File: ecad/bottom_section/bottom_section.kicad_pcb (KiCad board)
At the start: 2 copper layers, 100 x 57 mm, 50 parts, among them J1 JST PH 3, J3 JST PH 3, J5 Conn_01x08, SW1 SW_Push, SW10 SW_Push, SW2 SW_Push, SW3 SW_Push, SW4 SW_Push, SW5 SW_Push, SW6 SW_Push, SW7 SW_Push, SW8 SW_Push, SW9 SW_Push

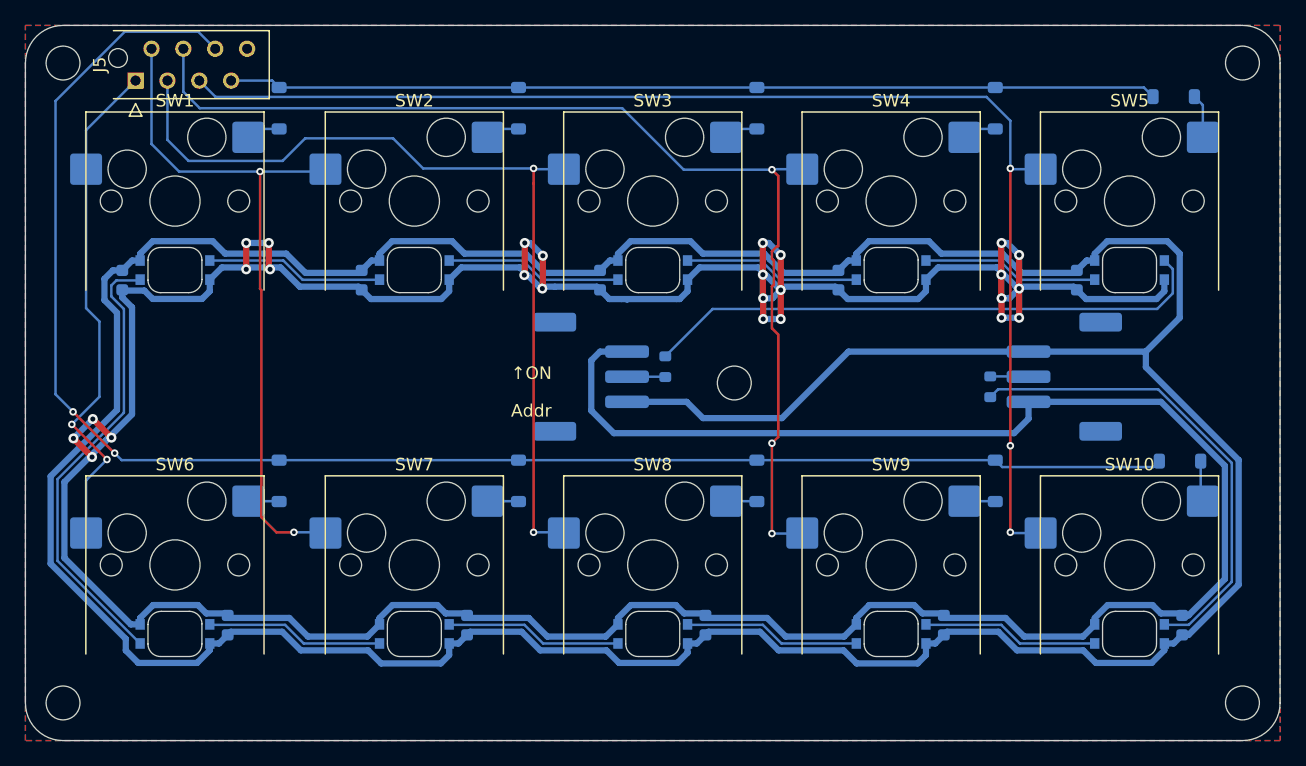
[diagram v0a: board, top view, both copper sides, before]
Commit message: Uses LED Matrix controller on all board.
It simplifies so much the design for a small cost.
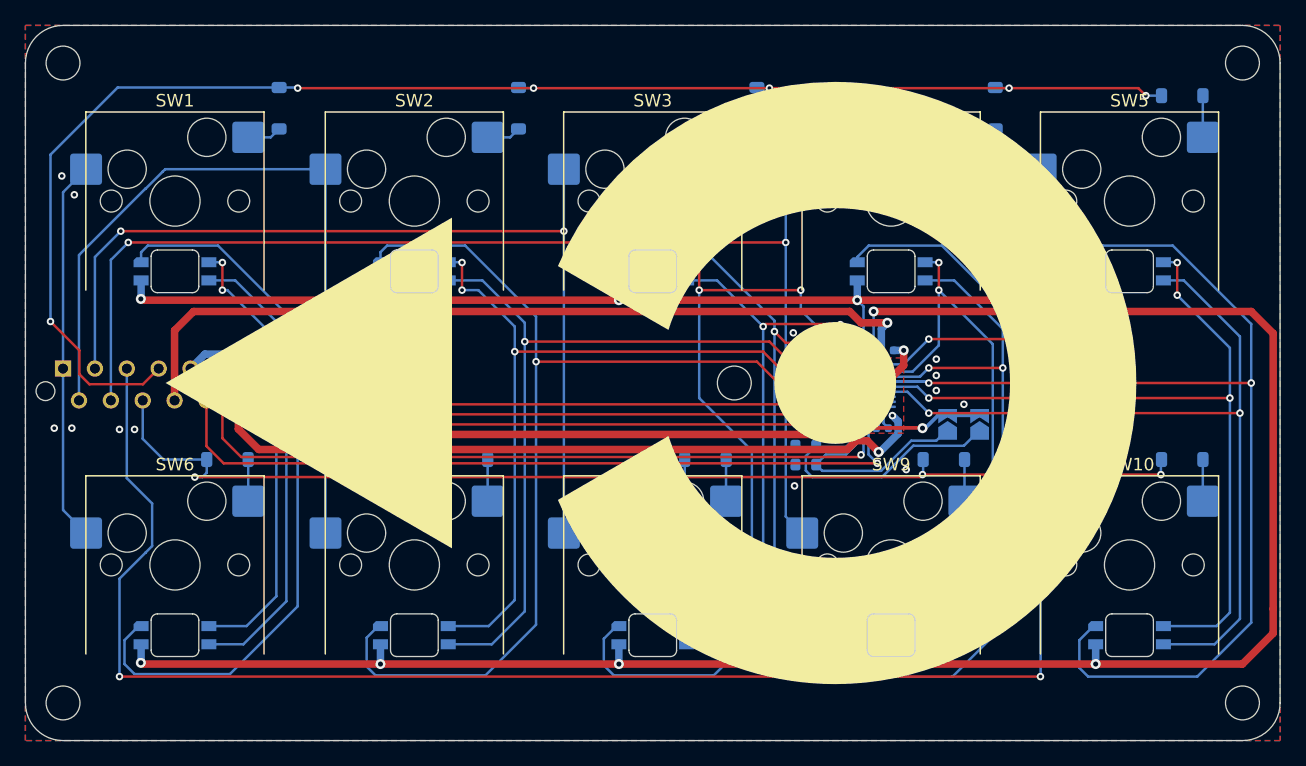
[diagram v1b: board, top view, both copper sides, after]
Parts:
- removed C1, C10, C6, C7, C8, C9: 100n, Capacitor_SMD:C_0603_1608Metric
- removed J3: JST PH 3, woodpecker:JST_PH_S3B-PH-SM4-TB_1x03-1MP_P2.00mm_Horizontal
- removed J5: Conn_01x08, Connector_TE-Connectivity:TE_Micro-MaTch_215079-8_2x04_P1.27mm_Vertical
- removed R7, R8: 33, Resistor_SMD:R_0603_1608Metric
- added JP1: SolderJumper_2_Open, Jumper:SolderJumper-2_P1.3mm_Open_TrianglePad1.0x1.5mm, B.Cu at (123.5, 58.8)
- added JP2: SolderJumper_2_Open, Jumper:SolderJumper-2_P1.3mm_Open_TrianglePad1.0x1.5mm, B.Cu at (126.0, 58.8)
- added R1: 10k, Resistor_SMD:R_0603_1608Metric, B.Cu at (112.2, 62.0)
- added R2: 10k, Resistor_SMD:R_0603_1608Metric, B.Cu at (112.2, 60.5)
- added REF**: OSHW-Logo_11.4x12mm_SilkScreen, Symbol:OSHW-Logo_11.4x12mm_SilkScreen, B.Cu at (90.9, 77.3)
- added U2: LP5864, woodpecker:Texas_LP586X_VQFN-32-1EP_4x4mm_P0.4mm_EP2.8x2.8mm_ThermalVias, B.Cu at (117.0, 56.0)
- added kibuzzard-68CC277E: G***, kibuzzard-68CC277E, B.Cu at (124.8, 56.4)
- added kibuzzard-68CC27A1: G***, kibuzzard-68CC27A1, B.Cu at (127.9, 60.1)
- added kibuzzard-68CC27B2: G***, kibuzzard-68CC27B2, B.Cu at (131.1, 58.8)
- added kibuzzard-68CC27E6: G***, kibuzzard-68CC27E6, B.Cu at (60.0, 51.2)
- added kibuzzard-68CC2926: G***, kibuzzard-68CC2926, B.Cu at (141.1, 53.3)
- C2, C3, C5: value 100n -> 1u; footprint Capacitor_SMD:C_0603_1608Metric -> Capacitor_SMD:C_0402_1005Metric
- C4: value 100n -> 1n; footprint Capacitor_SMD:C_0603_1608Metric -> Capacitor_SMD:C_0402_1005Metric
- D1, D11, D13, D15, D17, D19, D3, D5, D7, D9: value IN-PI32TAR -> LED_BGRA; footprint woodpecker:LED_Inolux_IN-PI32TAR_PLCC4_3.2x2.8mm_P1.5mm -> woodpecker:LED_Inolux_IN-PI32TRRRGB_PLCC4_3.2x2.8mm_P1.5mm
- J1: value JST PH 3 -> Micro-MaTch 2x06; footprint woodpecker:JST_PH_S3B-PH-SM4-TB_1x03-1MP_P2.00mm_Horizontal -> Connector_TE-Connectivity:TE_Micro-MaTch_1-215079-2_2x06_P1.27mm_Vertical
- moved J1 42.1 mm to (53.0, 54.4), turned to -90 degrees
- moved C2 38.4 mm to (113.5, 58.6)
- moved C3 23.6 mm to (118.7, 52.9), turned to 0 degrees
- moved C5 19.5 mm to (118.3, 59.1), turned to 180 degrees
- moved C4 11.8 mm to (114.9, 59.1), turned to 180 degrees
- moved D12 4.46 mm to (66.1, 61.6), turned to 0 degrees
- moved D14 4.44 mm to (85.2, 61.6), turned to 0 degrees
- moved D16 4.44 mm to (104.2, 61.6), turned to 0 degrees
- moved D18 4.44 mm to (123.2, 61.6), turned to 0 degrees
- moved D10 0.68 mm to (142.2, 32.6)
- moved D20 0.22 mm to (142.2, 61.6)
- moved D1 0.10 mm to (61.9, 46.6), turned to 180 degrees
- moved D3 0.10 mm to (81.0, 46.6), turned to 180 degrees
- moved D5 0.10 mm to (100.0, 46.6), turned to 180 degrees
- moved D7 0.10 mm to (119.0, 46.6), turned to 180 degrees
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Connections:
- C2 pad 1: +5V -> +3V3
- C4 pad 1: +5V -> +3V3
- C5 pad 1: +5V -> Net-(U2-VCAP)
- D1 pad 1: +5V -> /C1_LEDB
- D1 pad 2: /KeyboardKey_COL1/DOUT -> /C1_LEDG
- D1 pad 3: GND -> /C1_LEDR
- D1 pad 4: /KeyboardKey_COL1/DIN -> /R5_LEDA
- D11 pad 1: +5V -> /C1_LEDB
- D11 pad 2: /KeyboardKey_COL6/DOUT -> /C1_LEDG
- D11 pad 3: GND -> /C1_LEDR
- D11 pad 4: /KeyboardKey_COL1/DOUT -> /R6_LEDA
- D13 pad 1: +5V -> /C2_LEDB
- D13 pad 2: /KeyboardKey_COL7/DOUT -> /C2_LEDG
- D13 pad 3: GND -> /C2_LEDR
- D13 pad 4: /KeyboardKey_COL6/DOUT -> /R6_LEDA
- D15 pad 1: +5V -> /C3_LEDB
- D15 pad 2: /KeyboardKey_COL8/DOUT -> /C3_LEDG
- D15 pad 3: GND -> /C3_LEDR
- D15 pad 4: /KeyboardKey_COL7/DOUT -> /R6_LEDA
- D17 pad 1: +5V -> /C4_LEDB
- D17 pad 2: /KeyboardKey_COL10/DIN -> /C4_LEDG
- D17 pad 3: GND -> /C4_LEDR
- D17 pad 4: /KeyboardKey_COL8/DOUT -> /R6_LEDA
- D19 pad 1: +5V -> /C5_LEDB
- D19 pad 2: /KeyboardKey_COL10/DOUT -> /C5_LEDG
- D19 pad 3: GND -> /C5_LEDR
- D19 pad 4: /KeyboardKey_COL10/DIN -> /R6_LEDA
- D3 pad 1: +5V -> /C2_LEDB
- D3 pad 2: /KeyboardKey_COL1/DIN -> /C2_LEDG
- D3 pad 3: GND -> /C2_LEDR
- D3 pad 4: /KeyboardKey_COL2/DIN -> /R5_LEDA
- D5 pad 1: +5V -> /C3_LEDB
- D5 pad 2: /KeyboardKey_COL2/DIN -> /C3_LEDG
- D5 pad 3: GND -> /C3_LEDR
- D5 pad 4: /KeyboardKey_COL3/DIN -> /R5_LEDA
- D7 pad 1: +5V -> /C4_LEDB
- D7 pad 2: /KeyboardKey_COL3/DIN -> /C4_LEDG
- D7 pad 3: GND -> /C4_LEDR
- D7 pad 4: /KeyboardKey_COL4/DIN -> /R5_LEDA
- D9 pad 1: +5V -> /C5_LEDB
- D9 pad 2: /KeyboardKey_COL4/DIN -> /C5_LEDG
- D9 pad 3: GND -> /C5_LEDR
- D9 pad 4: /KeyboardKey_COL5/DIN -> /R5_LEDA
- J1 pad 1: +5V -> /COL1
- J1 pad 2: /DIN -> /COL2
- J1 pad 3: GND -> /COL3
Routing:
- net GND: track 350.3 -> 74.9 mm, vias 26 -> 19
- net +5V: track 308.8 -> 67.0 mm, vias 0 -> 1
- net /R6_LEDA: track 0.00 -> 159.8 mm, vias 0 -> 6
- net /C1_LEDB: track 0.00 -> 102.7 mm, vias 0 -> 2
- net /C5_LEDB: track 0.00 -> 91.3 mm, vias 0 -> 2
- net /R5_LEDA: track 0.00 -> 89.2 mm, vias 0 -> 5
- net /C2_LEDB: track 0.00 -> 84.7 mm, vias 0 -> 2
- net /C1_LEDG: track 0.00 -> 81.7 mm, vias 0 -> 4
- net /C1_LEDR: track 0.00 -> 81.6 mm, vias 0 -> 2
- net +3V3: track 0.00 -> 73.5 mm, vias 0 -> 3
- net /C4_LEDB: track 0.00 -> 70.5 mm, vias 0 -> 2
- net /C5_LEDR: track 0.00 -> 65.9 mm, vias 0 -> 2
- net /C3_LEDB: track 0.00 -> 65.8 mm, vias 0 -> 2
- net /C2_LEDR: track 0.00 -> 64.1 mm, vias 0 -> 2
- net /C5_LEDG: track 0.00 -> 63.9 mm, vias 0 -> 4
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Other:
- board text added: "© Copyright 2025 Alexandre Tuleu"
- board text removed: "Addr"
- board text removed: "↑ON"

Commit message: Updated Controller for I2C controlled LED Matrices
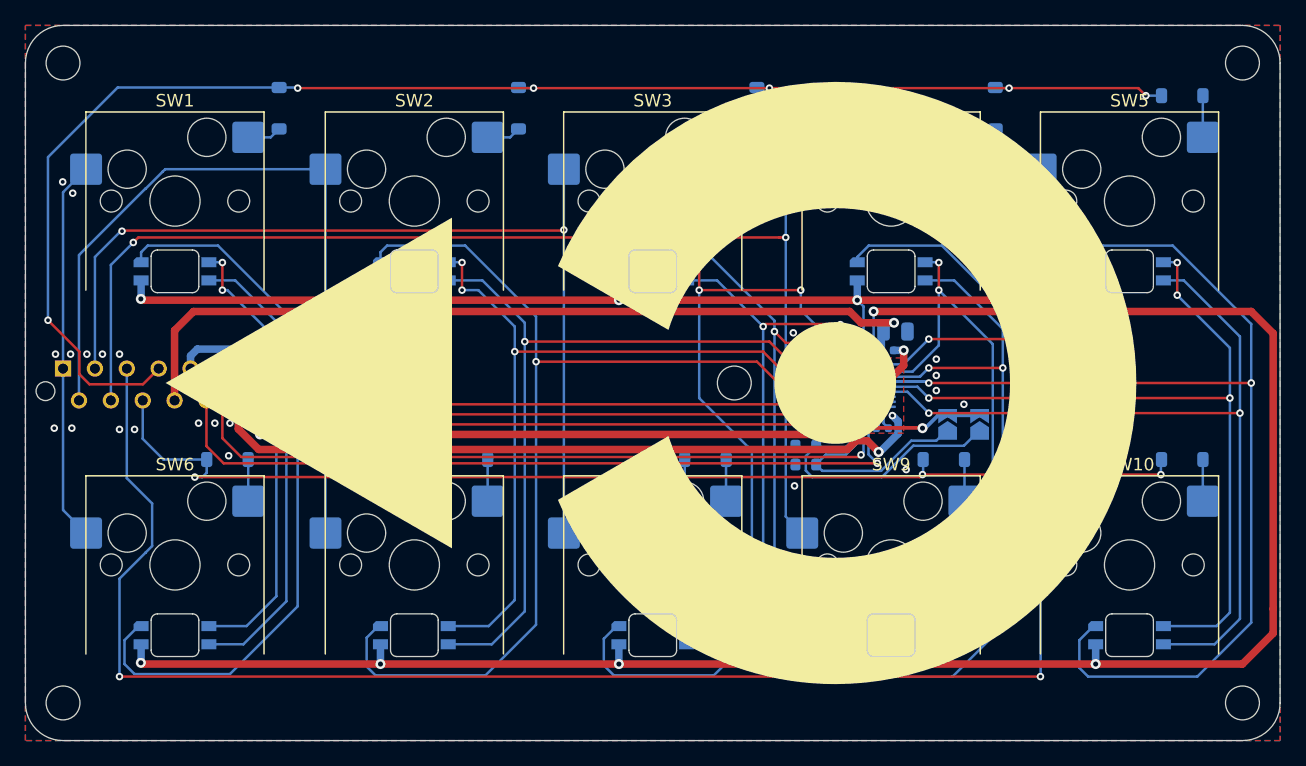
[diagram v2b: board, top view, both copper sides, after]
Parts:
- added C6: 22u, Capacitor_SMD:C_0805_2012Metric, B.Cu at (119.3, 51.4)
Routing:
- net +3V3: track 73.5 -> 75.6 mm
- net +5V: track 67.0 -> 68.0 mm
- net GND: vias 19 -> 28

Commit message: Outputs new  step files
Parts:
- J1: footprint Connector_TE-Connectivity:TE_Micro-MaTch_1-215079-2_2x06_P1.27mm_Vertical -> woodpecker:TE_Micro-MaTch_1-215079-2_2x06_P1.27mm_Vertical
- R1, R2: value 10k -> 33k
